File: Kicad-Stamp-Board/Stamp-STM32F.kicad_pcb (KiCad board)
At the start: 2 copper layers, 70 x 84 mm, 70 parts, among them J1 +3.3V, J2 GND, J3 Serial, J4 BOOT1, SW1 Reset, SW2 BOOT, U1 STM32Fxxx, U2 ICL3221, Y1 32.768KHz

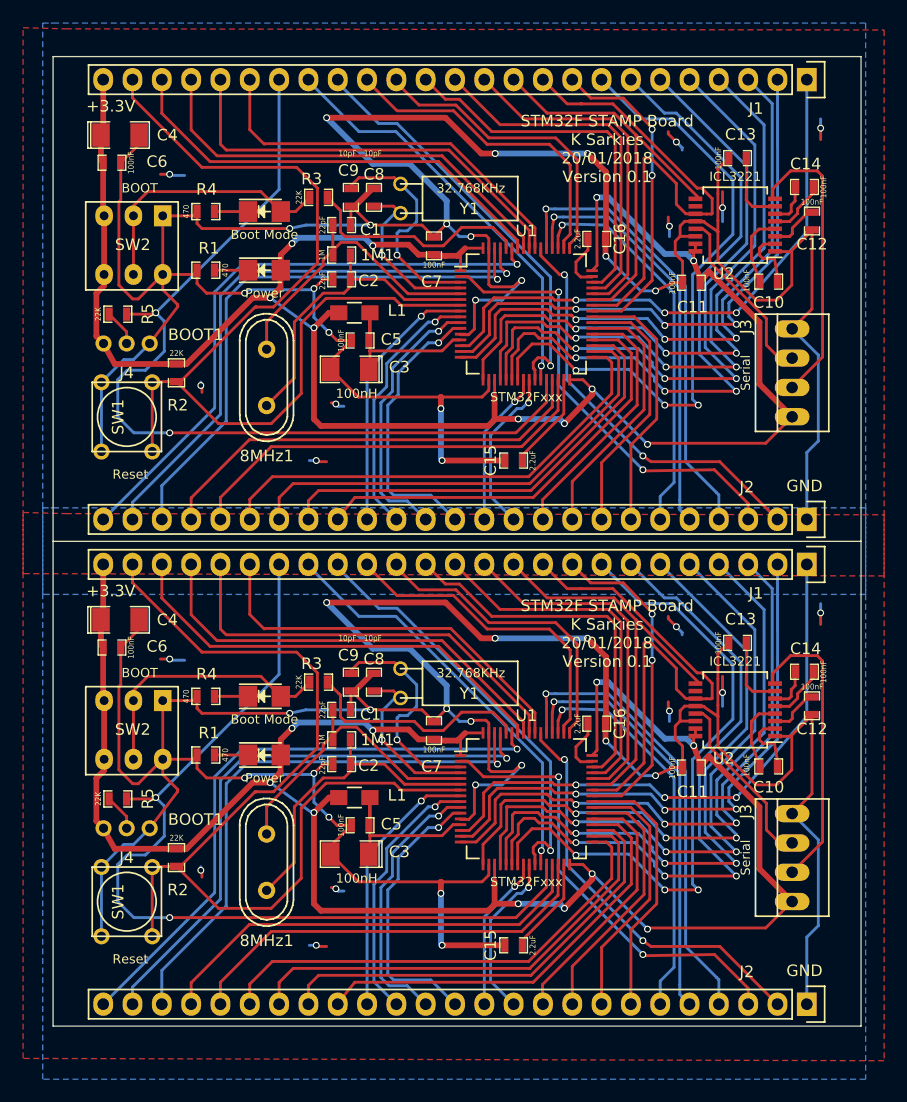
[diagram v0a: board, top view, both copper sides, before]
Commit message: Update PCB to add a jumper on each of pins 48 and 18 to accommodate additional STM32 families.
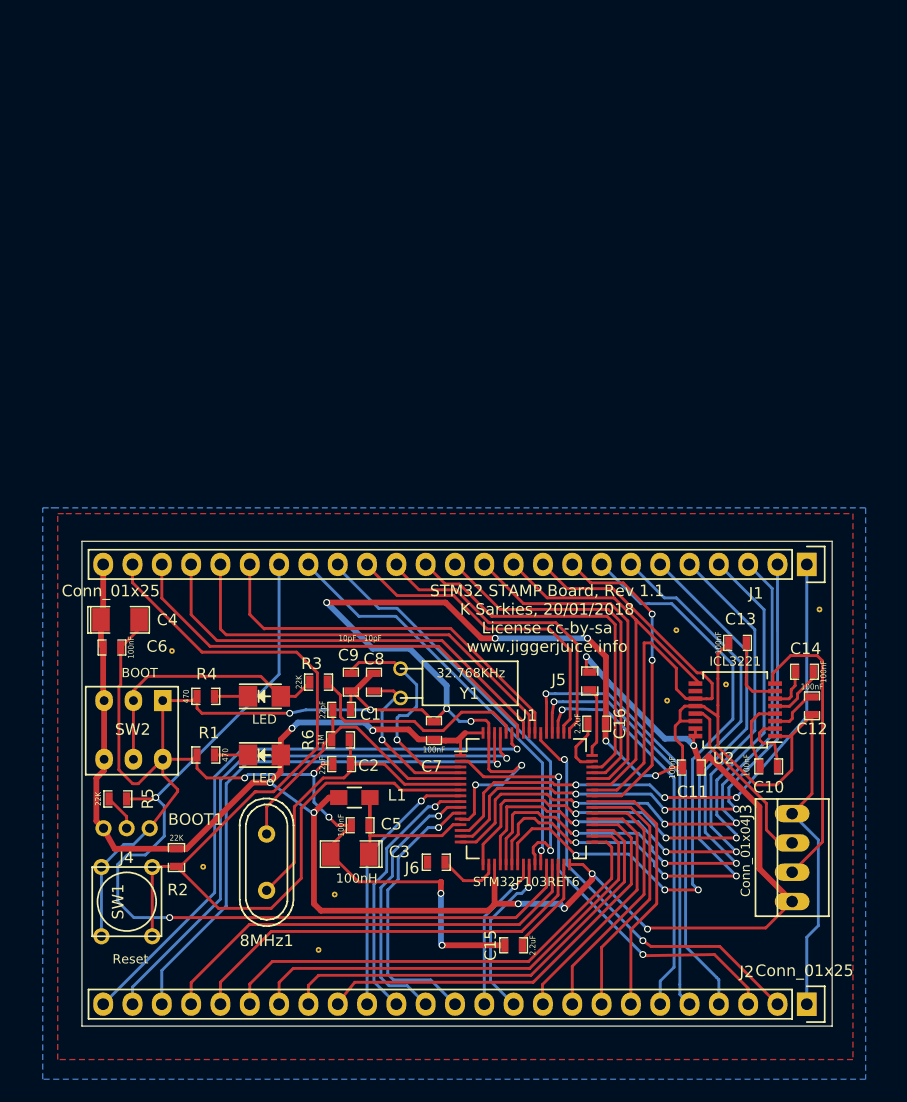
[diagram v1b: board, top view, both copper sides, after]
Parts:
- removed 1M1 (x2): 1M, stamp-stm32f:SM0603_Resistor
- removed the 8MHz1 at (131.0, 60.0)
- removed the C1 at (137.5, 46.8)
- removed the C10 at (174.5, 51.7)
- removed the C11 at (167.8, 51.8)
- removed the C12 at (178.2, 46.5)
- removed the C13 at (171.8, 41.0)
- removed the C14 at (177.6, 43.5)
- removed the C15 at (152.4, 67.2)
- removed the C16 at (159.6, 48.0)
- removed the C2 at (137.5, 51.5)
- removed the C3 at (138.2, 59.3)
- removed the C4 at (118.3, 39.0)
- removed the C5 at (139.1, 56.8)
- removed the C6 at (117.6, 41.4)
- removed the C7 at (145.5, 48.6)
- removed the C8 at (140.3, 44.4)
- removed the C9 at (138.3, 44.4)
- removed the D1 at (130.8, 50.7)
- removed the D2 at (130.8, 45.6)
- removed the J1 at (177.8, 34.2)
- removed the J2 at (177.8, 72.3)
- removed the J3 at (176.5, 59.6)
- removed the J4 at (118.9, 57.1)
- removed the L1 at (138.6, 54.4)
- removed the R1 at (125.7, 50.7)
- removed the R2 at (123.2, 59.6)
- removed the R3 at (135.5, 44.4)
- removed the R4 at (125.7, 45.6)
- removed the R5 at (118.1, 54.5)
- removed the SW1 at (118.9, 63.4)
- removed the SW2 at (122.0, 46.0)
- removed the U1 at (153.5, 54.5)
- removed the U2 at (171.6, 46.8)
- removed the Y1 at (142.6, 44.5)
- added J10: Conn_01x01, stamp-stm32f:THROUGHVIA, F.Cu at (136.9, 104.8)
- added J11: Conn_01x01, stamp-stm32f:THROUGHVIA, F.Cu at (170.8, 86.6)
- added J12: Conn_01x01, stamp-stm32f:THROUGHVIA, F.Cu at (178.9, 80.1)
- added J13: Conn_01x01, stamp-stm32f:THROUGHVIA, F.Cu at (125.5, 102.4)
- added J5: Jumper, stamp-stm32f:SM0603_Resistor, F.Cu at (159.0, 86.3)
- added J6: Jumper, stamp-stm32f:SM0603_Resistor, F.Cu at (145.7, 102.0)
- added J7: Conn_01x01, stamp-stm32f:THROUGHVIA, F.Cu at (122.8, 83.7)
- added J8: Conn_01x01, stamp-stm32f:THROUGHVIA, F.Cu at (165.7, 88.0)
- added J9: Conn_01x01, stamp-stm32f:THROUGHVIA, F.Cu at (135.5, 109.6)
- added R6: 1M, stamp-stm32f:SM0603_Resistor, F.Cu at (137.4, 91.4)
- added Ref**: Val**, stamp-stm32f:THROUGHVIA, F.Cu at (166.5, 81.9)
- D1: value Power -> LED
- D2: value Boot Mode -> LED
- J1: value +3.3V -> Conn_01x25
- J2: value GND -> Conn_01x25
- J3: value Serial -> Conn_01x04
- U1: value STM32Fxxx -> STM32F103RET6
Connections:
- U1 pad 18: Earth -> Net-(J6-Pad1)
- U1 pad 48: 3.3V -> Net-(J5-Pad1)
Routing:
- net Earth: track 544.9 -> 267.1 mm, vias 32 -> 16
- net 3.3V: track 344.4 -> 169.0 mm, vias 20 -> 10
- net RESET: track 172.7 -> 86.4 mm
- net PB2: track 159.9 -> 79.9 mm, vias 4 -> 2
- net PA6: track 118.9 -> 59.5 mm, vias 6 -> 3
- net PA5: track 115.8 -> 57.9 mm, vias 6 -> 3
- net PA4: track 113.5 -> 56.8 mm, vias 6 -> 3
- net PA7: track 112.9 -> 56.4 mm, vias 6 -> 3
- net PA3: track 111.5 -> 55.7 mm, vias 6 -> 3
- net PA2: track 107.7 -> 53.8 mm, vias 6 -> 3
- net PB7: track 105.2 -> 52.6 mm, vias 2 -> 1
- net PA1: track 102.0 -> 51.0 mm, vias 6 -> 3
- net PB8: track 101.5 -> 50.7 mm, vias 2 -> 1
- net PA0: track 99.7 -> 49.9 mm, vias 6 -> 3
- net PB9: track 97.2 -> 48.6 mm, vias 2 -> 1
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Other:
- board size 70 x 84 mm -> 65 x 42 mm
- board text added: "STM32 STAMP Board, Rev 1.1 K Sarkies, 20/01/2018 License cc-by-sa www.jiggerjuice.info"
- board text removed: "STM32F STAMP Board K Sarkies 20/01/2018 Version 0.1"

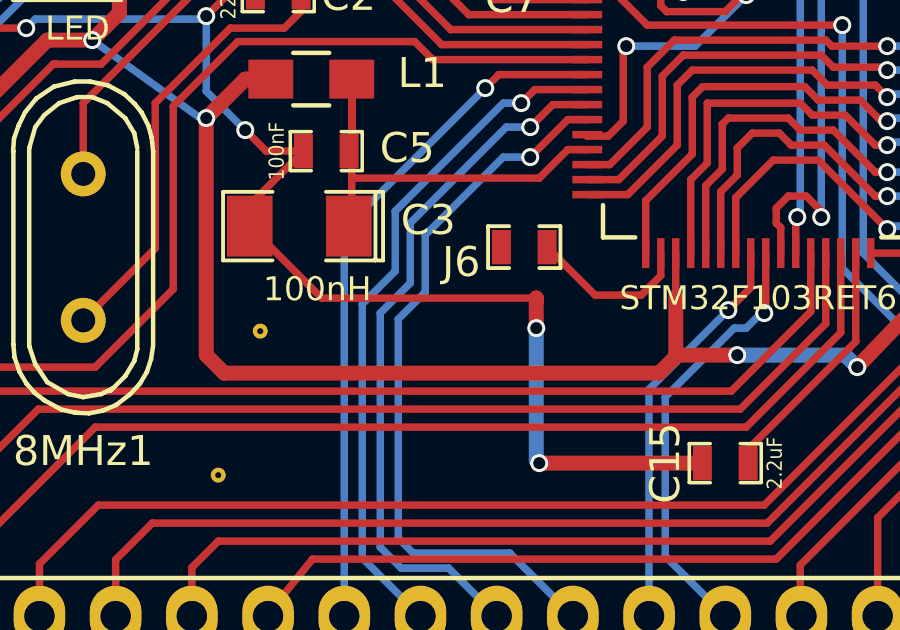
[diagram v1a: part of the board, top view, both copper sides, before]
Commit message: Add another jumper to cater for STM32F051.
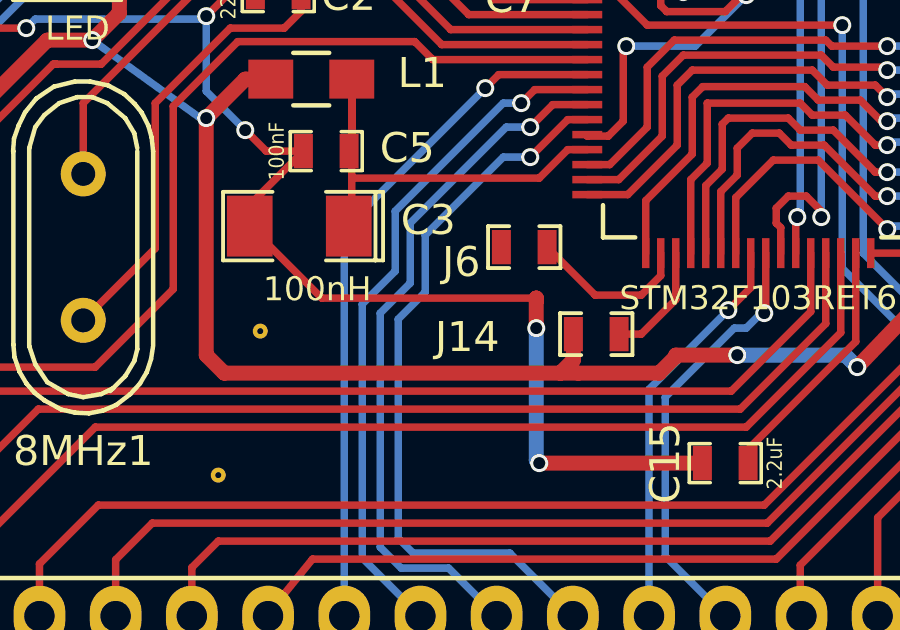
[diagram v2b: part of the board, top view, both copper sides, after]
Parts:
- added J14: Jumper, stamp-stm32f:SM0603_Resistor, F.Cu at (148.1, 104.9)
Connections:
- U1 pad 19: 3.3V -> Net-(J14-Pad1)
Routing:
- net Net-(J14-Pad1): track 0.00 -> 3.91 mm
- net 3.3V: track 169.0 -> 167.2 mm
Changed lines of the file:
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@@
 (kicad_pcb (version 4) (host pcbnew 4.0.7-e2-6376~58~ubuntu14.04.1)
   (general
-    (links 139)
+    (links 140)
     (no_connects 0)
     (area 111.6 71.3 183.64762 120.800001)
     (thickness 1.6)
     (drawings 5)
-    (tracks 863)
+    (tracks 868)
     (zones 0)
-    (modules 45)
-    (nets 74)
+    (modules 46)
+    (nets 75)
   )
   (page A4)
   (layers
-    (0 F.Cu signal hide)
-    (31 B.Cu signal hide)
+    (0 F.Cu signal)
+    (31 B.Cu signal)
     (32 B.Adhes user hide)
     (33 F.Adhes user hide)
@@
   )
   (setup
-    (last_trace_width 0.25)
+    (last_trace_width 0.5)
     (user_trace_width 0.5)
     (trace_clearance 0.2)
@@
   (net 72 "Net-(J5-Pad1)")
   (net 73 "Net-(J6-Pad1)")
+  (net 74 "Net-(J14-Pad1)")
   (net_class Default "This is the default net class."
     (clearance 0.2)
@@
     (add_net "Net-(D2-Pad1)")
     (add_net "Net-(D2-Pad2)")
+    (add_net "Net-(J14-Pad1)")
     (add_net "Net-(J3-Pad2)")
     (add_net "Net-(J3-Pad3)")
@@
       (net 73 "Net-(J6-Pad1)"))
     (pad 19 smd rect (at -2.75 5.7 90) (size 1 0.25) (layers F.Cu F.Paste F.Mask)
-      (net 3 3.3V))
+      (net 74 "Net-(J14-Pad1)"))
     (pad 20 smd rect (at -2.25 5.7 90) (size 1 0.25) (layers F.Cu F.Paste F.Mask)
       (net 19 PA4))
@@
     (pad 1 thru_hole circle (at 0 0) (size 0.5 0.5) (drill 0.2) (layers *.Cu *.Mask F.SilkS)
       (zone_connect 2))
+  )
+  (module stamp-stm32f:SM0603_Resistor (layer F.Cu)
+    (at 148.1 104.9 180)
+    (attr smd)
+    (fp_text reference J14 (at 4.3 -0.1 360) (layer F.SilkS)
+      (effects (font (size 1 1) (thickness 0.15)))
+    )
+    (fp_text value Jumper (at -1.69926 0 270) (layer F.SilkS) hide
+      (effects (font (size 0.508 0.4572) (thickness 0.1143)))
+    )
+    (fp_line (start -0.50038 -0.6985) (end -1.2065 -0.6985) (layer F.SilkS) (width 0.127))
+    (fp_line (start -1.2065 -0.6985) (end -1.2065 0.6985) (layer F.SilkS) (width 0.127))
+    (fp_line (start -1.2065 0.6985) (end -0.50038 0.6985) (layer F.SilkS) (width 0.127))
+    (fp_line (start 1.2065 -0.6985) (end 0.50038 -0.6985) (layer F.SilkS) (width 0.127))
+    (fp_line (start 1.2065 -0.6985) (end 1.2065 0.6985) (layer F.SilkS) (width 0.127))
+    (fp_line (start 1.2065 0.6985) (end 0.50038 0.6985) (layer F.SilkS) (width 0.127))
+    (pad 1 smd rect (at -0.762 0 180) (size 0.635 1.143) (layers F.Cu F.Paste F.Mask)
+      (net 74 "Net-(J14-Pad1)"))
+    (pad 2 smd rect (at 0.762 0 180) (size 0.635 1.143) (layers F.Cu F.Paste F.Mask)
+      (net 3 3.3V))
+    (model smd\resistors\R0603.wrl
+      (at (xyz 0 0 0.001000000047497451))
+      (scale (xyz 0.5 0.5 0.5))
+      (rotate (xyz 0 0 0))
+    )
   )
   (gr_text "STM32 STAMP Board, Rev 1.1\nK Sarkies, 20/01/2018\nLicense cc-by-sa\nwww.jiggerjuice.info" (at 155.3 80.9) (layer F.SilkS)
@@
   (segment (start 139.95 99.7) (end 139.95 101.201) (width 0.25) (layer F.Cu) (net 2))
   (segment (start 139.95 101.201) (end 139.851 101.3) (width 0.25) (layer F.Cu) (net 2))
+  (segment (start 147.338 104.9) (end 147.338 105.762) (width 0.5) (layer F.Cu) (net 3))
+  (segment (start 147.338 105.762) (end 146.9 106.2) (width 0.5) (layer F.Cu) (net 3))
   (segment (start 158.7 85.238) (end 158.7 84.2) (width 0.25) (layer F.Cu) (net 3))
   (via (at 158.7 84.2) (size 0.6) (drill 0.4) (layers F.Cu B.Cu) (net 3))
@@
   (segment (start 116.25 94.715) (end 116.25 98.44) (width 0.5) (layer F.Cu) (net 3))
   (segment (start 116.92 94.045) (end 116.25 94.715) (width 0.5) (layer F.Cu) (net 3))
-  (segment (start 152.8 105.6) (end 156.4 105.6) (width 0.5) (layer B.Cu) (net 3))
-  (via (at 152.8 105.6) (size 0.6) (drill 0.4) (layers F.Cu B.Cu) (net 3))
-  (segment (start 150.75 105.6) (end 152.8 105.6) (width 0.5) (layer F.Cu) (net 3))
   (via (at 156.8 106) (size 0.6) (drill 0.4) (layers F.Cu B.Cu) (net 3))
   (segment (start 156.8 106) (end 159.2 103.5) (width 0.5) (layer F.Cu) (net 3))
   (segment (start 159.2 103.5) (end 159.2 103) (width 0.5) (layer F.Cu) (net 3))
-  (segment (start 156.4 105.6) (end 156.8 106) (width 0.5) (layer B.Cu) (net 3))
   (segment (start 146.512 91.462) (end 147.538 91.462) (width 0.5) (layer F.Cu) (net 3))
   (segment (start 147.538 91.462) (end 148.2 90.8) (width 0.5) (layer F.Cu) (net 3))
@@
   (segment (start 147.8 91.2) (end 148.2 90.8) (width 0.25) (layer F.Cu) (net 3))
   (segment (start 148.2 90.8) (end 149.75 90.8) (width 0.25) (layer F.Cu) (net 3))
-  (segment (start 150.75 105.5) (end 150.75 103.65) (width 0.5) (layer F.Cu) (net 3))
-  (segment (start 150.75 102.2) (end 150.75 103.65) (width 0.25) (layer F.Cu) (net 3))
-  (segment (start 150.75 105.5) (end 150.75 105.6) (width 0.25) (layer F.Cu) (net 3))
   (segment (start 116.649 81) (end 116.649 83.211) (width 0.5) (layer F.Cu) (net 3))
   (segment (start 116.649 83.211) (end 116.838 83.4) (width 0.25) (layer F.Cu) (net 3))
@@
   (segment (start 168.562 93.8) (end 169.3 92.8) (width 0.5) (layer F.Cu) (net 3) (status 10))
   (segment (start 173.7 102.58) (end 176.53 105.41) (width 0.5) (layer F.Cu) (net 3))
-  (segment (start 150.75 105.6) (end 150.75 105.65) (width 0.5) (layer F.Cu) (net 3))
-  (segment (start 135.7 106.2) (end 135.1 105.6) (width 0.5) (layer F.Cu) (net 3))
-  (segment (start 150.2 106.2) (end 135.7 106.2) (width 0.5) (layer F.Cu) (net 3))
-  (segment (start 135.1 105.6) (end 135.1 97.7) (width 0.5) (layer F.Cu) (net 3))
-  (segment (start 150.75 105.65) (end 150.2 106.2) (width 0.5) (layer F.Cu) (net 3))
   (segment (start 132.22986 92.71) (end 132.22986 91.37014) (width 0.5) (layer F.Cu) (net 3))
   (segment (start 132.22986 91.37014) (end 133.2 90.4) (width 0.5) (layer F.Cu) (net 3))
@@
   (segment (start 132.2 94.2) (end 131.3 95.1) (width 0.5) (layer F.Cu) (net 3))
   (segment (start 136.4 96.4) (end 137.25 96.4) (width 0.5) (layer F.Cu) (net 3))
-  (segment (start 135.1 97.7) (end 136.4 96.4) (width 0.5) (layer F.Cu) (net 3))
-  (via (at 135.1 97.7) (size 0.6) (drill 0.4) (layers F.Cu B.Cu) (net 3))
-  (segment (start 134.9 97.7) (end 135.1 97.7) (width 0.25) (layer B.Cu) (net 3))
-  (segment (start 131.3 95.1) (end 134.9 97.7) (width 0.25) (layer B.Cu) (net 3))
   (via (at 131.3 95.1) (size 0.6) (drill 0.4) (layers F.Cu B.Cu) (net 3))
   (segment (start 145.3 91.462) (end 146.512 91.462) (width 0.5) (layer F.Cu) (net 3))
@@
   (segment (start 117.838 100.838) (end 123.19 100.838) (width 0.5) (layer F.Cu) (net 3))
   (segment (start 116.92 88) (end 116.92 93.08) (width 0.5) (layer F.Cu) (net 3))
+  (segment (start 135.1 97.7) (end 136.4 96.4) (width 0.5) (layer F.Cu) (net 3))
+  (segment (start 131.3 95.1) (end 134.9 97.7) (width 0.25) (layer B.Cu) (net 3))
+  (segment (start 152.8 105.6) (end 156.4 105.6) (width 0.5) (layer B.Cu) (net 3))
+  (via (at 152.8 105.6) (size 0.6) (drill 0.4) (layers F.Cu B.Cu) (net 3))
+  (segment (start 150.75 105.6) (end 152.8 105.6) (width 0.5) (layer F.Cu) (net 3))
+  (segment (start 156.4 105.6) (end 156.8 106) (width 0.5) (layer B.Cu) (net 3))
+  (segment (start 150.75 105.5) (end 150.75 105.6) (width 0.25) (layer F.Cu) (net 3))
+  (segment (start 150.75 105.6) (end 150.75 105.65) (width 0.5) (layer F.Cu) (net 3))
+  (segment (start 135.7 106.2) (end 135.1 105.6) (width 0.5) (layer F.Cu) (net 3))
+  (segment (start 150.2 106.2) (end 147.5 106.2) (width 0.5) (layer F.Cu) (net 3))
+  (segment (start 147.5 106.2) (end 146.9 106.2) (width 0.5) (layer F.Cu) (net 3))
+  (segment (start 146.9 106.2) (end 135.7 106.2) (width 0.5) (layer F.Cu) (net 3))
+  (segment (start 135.1 105.6) (end 135.1 97.7) (width 0.5) (layer F.Cu) (net 3))
+  (segment (start 150.75 105.65) (end 150.2 106.2) (width 0.5) (layer F.Cu) (net 3))
+  (via (at 135.1 97.7) (size 0.6) (drill 0.4) (layers F.Cu B.Cu) (net 3))
+  (segment (start 134.9 97.7) (end 135.1 97.7) (width 0.25) (layer B.Cu) (net 3))
   (segment (start 147.8 94.25) (end 143.85 94.25) (width 0.25) (layer F.Cu) (net 4))
   (segment (start 141 88.9) (end 142.13 87.77) (width 0.25) (layer B.Cu) (net 4))
@@
   (segment (start 149.6 103.6) (end 148.062 103.6) (width 0.25) (layer F.Cu) (net 73))
   (segment (start 150.25 102.95) (end 149.6 103.6) (width 0.25) (layer F.Cu) (net 73))
+  (segment (start 150.75 102.2) (end 150.75 103.75) (width 0.25) (layer F.Cu) (net 74))
+  (segment (start 149.6 104.9) (end 148.862 104.9) (width 0.25) (layer F.Cu) (net 74))
+  (segment (start 150.75 103.75) (end 149.6 104.9) (width 0.25) (layer F.Cu) (net 74))
   (zone (net 1) (net_name Earth) (layer F.Cu) (hatch edge 0.508)
     (connect_pads (clearance 0.508))
